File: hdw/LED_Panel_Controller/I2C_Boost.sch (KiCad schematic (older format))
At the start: 2 parts

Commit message: made a lot more schematic progress
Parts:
- C?, U?: Configuration (none) -> DNP
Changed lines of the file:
@@
 F 3 "https://www.analog.com/media/en/technical-documentation/data-sheets/1694fa.pdf" H 5200 4060 60  0001 C CNN
 F 4 "LTC1694CS5#TRPBFCT-ND" H 5400 3510 60  0001 C CNN "Digi-Key PN"
+F 5 "DNP" H 5300 3300 50  0000 C CNN "Configuration"
 	1    5300 3760
 	1    0    0    -1
@@
 F 6 "X7R" H 4190 3680 50  0000 R CNN "Dielectric"
 F 7 "490-10701-1-ND" H 4765 4280 60  0001 C CNN "Digi-Key PN"
+F 8 "DNP" H 4110 3970 50  0000 C CNN "Configuration"
 	1    4340 3780
 	1    0    0    -1

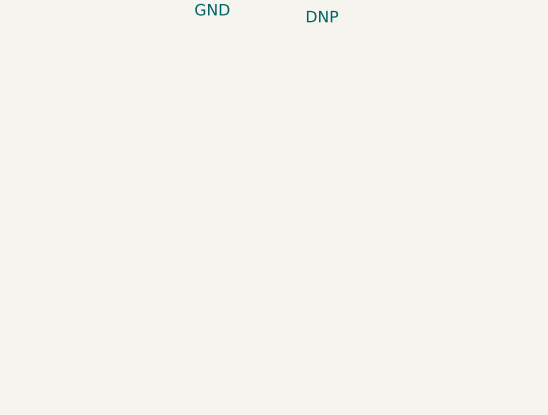
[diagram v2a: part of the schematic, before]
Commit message: assigned a lot of nets to MCU pins
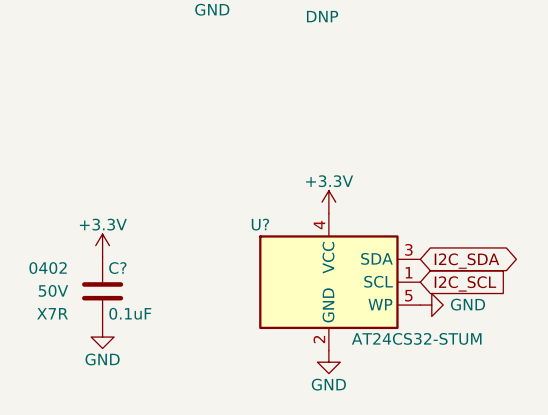
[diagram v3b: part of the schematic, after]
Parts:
- added C?: 0.1uF, Capacitors_SMD:C_0402, symbol Custom_Library:C_Custom
- added U?: AT24CS32-STUM, Package_TO_SOT_SMD:SOT-23-5, symbol Memory_EEPROM:AT24CS32-STUM
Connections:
- net +3V3: now also C?.1, U?.4 (VCC)
- net GND: now also C?.2, U?.2 (GND), U?.5 (WP)
- net I2C_SCL: now also U?.1 (SCL)
- net I2C_SDA: now also U?.3 (SDA)
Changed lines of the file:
@@
 	1    0    0    -1
 $EndComp
+$Comp
+L Memory_EEPROM:AT24CS32-STUM U?
+U 1 1 601A8ABF
+P 5330 5380
+AR Path="/5F5829EF/601A8ABF" Ref="U?"  Part="1"
+AR Path="/5F582A7C/601A8ABF" Ref="U?"  Part="1"
+F 0 "U?" H 5030 5630 50  0000 C CNN
+F 1 "AT24CS32-STUM" H 5430 5130 50  0000 L CNN
+F 2 "Package_TO_SOT_SMD:SOT-23-5" H 5330 5380 50  0001 C CNN
+F 3 "http://ww1.microchip.com/downloads/en/DeviceDoc/Atmel-8869-SEEPROM-AT24CS32-Datasheet.pdf" H 5330 5380 50  0001 C CNN
+	1    5330 5380
+	1    0    0    -1
+$EndComp
+$Comp
+L power:GND #PWR?
+U 1 1 601A8AC5
+P 5330 5680
+AR Path="/5F5829EF/601A8AC5" Ref="#PWR?"  Part="1"
+AR Path="/5F582A7C/601A8AC5" Ref="#PWR?"  Part="1"
+F 0 "#PWR?" H 5330 5430 50  0001 C CNN
+F 1 "GND" H 5330 5530 50  0000 C CNN
+F 2 "" H 5330 5680 50  0001 C CNN
+F 3 "" H 5330 5680 50  0001 C CNN
+	1    5330 5680
+	1    0    0    -1
+$EndComp
+$Comp
+L power:+3.3V #PWR?
+U 1 1 601A8ACB
+P 5330 5080
+AR Path="/5F5829EF/601A8ACB" Ref="#PWR?"  Part="1"
+AR Path="/5F582A7C/601A8ACB" Ref="#PWR?"  Part="1"
+F 0 "#PWR?" H 5330 4930 50  0001 C CNN
+F 1 "+3.3V" H 5330 5220 50  0000 C CNN
+F 2 "" H 5330 5080 50  0001 C CNN
+F 3 "" H 5330 5080 50  0001 C CNN
+	1    5330 5080
+	1    0    0    -1
+$EndComp
+$Comp
+L power:GND #PWR?
+U 1 1 601A97E7
+P 4340 5570
+F 0 "#PWR?" H 4340 5320 50  0001 C CNN
+F 1 "GND" H 4340 5420 50  0000 C CNN
+F 2 "" H 4340 5570 50  0001 C CNN
+F 3 "" H 4340 5570 50  0001 C CNN
+	1    4340 5570
+	1    0    0    -1
+$EndComp
+$Comp
+L Custom_Library:C_Custom C?
+U 1 1 601A97F2
+P 4340 5420
+AR Path="/5BAAE16C/601A97F2" Ref="C?"  Part="1"
+AR Path="/5BB181D8/601A97F2" Ref="C?"  Part="1"
+AR Path="/5BB2595E/601A97F2" Ref="C?"  Part="1"
+AR Path="/5BAAE0FA/601A97F2" Ref="C?"  Part="1"
+AR Path="/5BB86F23/601A97F2" Ref="C?"  Part="1"
+AR Path="/5C1D5C9E/601A97F2" Ref="C?"  Part="1"
+AR Path="/5CB6F1ED/601A97F2" Ref="C?"  Part="1"
+AR Path="/5E939CFF/601A97F2" Ref="C?"  Part="1"
+AR Path="/5E9E0E87/601A97F2" Ref="C?"  Part="1"
+AR Path="/5EAE2D66/601A97F2" Ref="C?"  Part="1"
+AR Path="/5EAE3021/601A97F2" Ref="C?"  Part="1"
+AR Path="/5F582A92/601A97F2" Ref="C?"  Part="1"
+AR Path="/5F582A7C/601A97F2" Ref="C?"  Part="1"
+F 0 "C?" H 4365 5520 50  0000 L CNN
+F 1 "0.1uF" H 4365 5320 50  0000 L CNN
+F 2 "Capacitors_SMD:C_0402" H 4378 5270 50  0001 C CNN
+F 3 "" H 4365 5520 50  0001 C CNN
+F 4 "0402" H 4190 5520 50  0000 R CNN "display_footprint"
+F 5 "50V" H 4190 5420 50  0000 R CNN "Voltage"
+F 6 "X7R" H 4190 5320 50  0000 R CNN "Dielectric"
+F 7 "490-10701-1-ND" H 4765 5920 60  0001 C CNN "Digi-Key PN"
+F 8 "" H 4110 5610 50  0001 C CNN "Configuration"
+	1    4340 5420
+	1    0    0    -1
+$EndComp
+$Comp
+L power:+3.3V #PWR?
+U 1 1 601A97F8
+P 4340 5270
+F 0 "#PWR?" H 4340 5120 50  0001 C CNN
+F 1 "+3.3V" H 4340 5410 50  0000 C CNN
+F 2 "" H 4340 5270 50  0001 C CNN
+F 3 "" H 4340 5270 50  0001 C CNN
+	1    4340 5270
+	1    0    0    -1
+$EndComp
+Text GLabel 5730 5380 2    50   Input ~ 0
+I2C_SCL
+Text GLabel 5730 5280 2    50   BiDi ~ 0
+I2C_SDA
+$Comp
+L power:GND #PWR?
+U 1 1 601AB410
+P 5730 5480
+AR Path="/5F5829EF/601AB410" Ref="#PWR?"  Part="1"
+AR Path="/5F582A7C/601AB410" Ref="#PWR?"  Part="1"
+F 0 "#PWR?" H 5730 5230 50  0001 C CNN
+F 1 "GND" V 5730 5350 50  0000 R CNN
+F 2 "" H 5730 5480 50  0001 C CNN
+F 3 "" H 5730 5480 50  0001 C CNN
+	1    5730 5480
+	0    -1   -1   0
+$EndComp
 $EndSCHEMATC

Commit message: more schematic development
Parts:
- added C?: 0.1uF, Capacitors_SMD:C_0402, symbol Custom_Library:C_Custom
- added DOC?: FIXME, symbol Custom_Library:I2C_Address
- added U?: MCP9804, Package_DFN_QFN:DFN-8-1EP_3x2mm_P0.5mm_EP1.3x1.5mm, symbol Sensor_Temperature:MCP9804_DFN
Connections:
- net +3V3: now also C?.1, U?.8 (VDD)
- net GND: now also C?.2, U?.4 (GND), U?.9 (EP/GND)
- net I2C_SCL: now also U?.2 (SCL)
- net I2C_SDA: now also U?.1 (SDA)
- no-connect marks 0 -> 1
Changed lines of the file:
@@
 Sheet 13 34
 Title "LED Panel Controller"
-Date "2020-12-23"
+Date "2021-03-24"
 Rev "A"
-Comp "Drew Maatman, Logan Wedel"
+Comp "Drew Maatman"
 Comment1 ""
 Comment2 ""
@@
 	0    -1   -1   0
 $EndComp
+$Comp
+L power:GND #PWR?
+U 1 1 6061CC13
+P 5340 2050
+AR Path="/5B3E071A/6061CC13" Ref="#PWR?"  Part="1"
+AR Path="/5E0652BA/6061CC13" Ref="#PWR?"  Part="1"
+AR Path="/5E0A0E29/6061CC13" Ref="#PWR?"  Part="1"
+AR Path="/5E052856/6061CC13" Ref="#PWR?"  Part="1"
+AR Path="/5EAE2D84/6061CC13" Ref="#PWR?"  Part="1"
+AR Path="/5F581B58/6061CC13" Ref="#PWR?"  Part="1"
+AR Path="/5F581B77/6061CC13" Ref="#PWR?"  Part="1"
+AR Path="/5F581BB7/6061CC13" Ref="#PWR?"  Part="1"
+AR Path="/5F582A7C/6061CC13" Ref="#PWR?"  Part="1"
+F 0 "#PWR?" H 5340 1800 50  0001 C CNN
+F 1 "GND" H 5340 1900 50  0000 C CNN
+F 2 "" H 5340 2050 50  0001 C CNN
+F 3 "" H 5340 2050 50  0001 C CNN
+	1    5340 2050
+	-1   0    0    -1
+$EndComp
+Wire Wire Line
+	5340 2050 5340 2010
+Wire Wire Line
+	5340 2010 5340 1970
+Wire Wire Line
+	5340 2010 5240 2010
+Wire Wire Line
+	5240 2010 5240 1970
+Connection ~ 5340 2010
+$Comp
+L power:+3.3V #PWR?
+U 1 1 6061CC1E
+P 5340 970
+AR Path="/5E0652BA/6061CC1E" Ref="#PWR?"  Part="1"
+AR Path="/5E0A0E29/6061CC1E" Ref="#PWR?"  Part="1"
+AR Path="/5E052856/6061CC1E" Ref="#PWR?"  Part="1"
+AR Path="/5EAE2D84/6061CC1E" Ref="#PWR?"  Part="1"
+AR Path="/5F581B58/6061CC1E" Ref="#PWR?"  Part="1"
+AR Path="/5F581B77/6061CC1E" Ref="#PWR?"  Part="1"
+AR Path="/5F581BB7/6061CC1E" Ref="#PWR?"  Part="1"
+AR Path="/5F582A7C/6061CC1E" Ref="#PWR?"  Part="1"
+F 0 "#PWR?" H 5340 820 50  0001 C CNN
+F 1 "+3.3V" H 5340 1110 50  0000 C CNN
+F 2 "" H 5340 970 50  0001 C CNN
+F 3 "" H 5340 970 50  0001 C CNN
+	1    5340 970
+	-1   0    0    -1
+$EndComp
+$Comp
+L Sensor_Temperature:MCP9804_DFN U?
+U 1 1 6061CC26
+P 5340 1470
+AR Path="/5B3E071A/6061CC26" Ref="U?"  Part="1"
+AR Path="/5E0652BA/6061CC26" Ref="U?"  Part="1"
+AR Path="/5E0A0E29/6061CC26" Ref="U?"  Part="1"
+AR Path="/5E052856/6061CC26" Ref="U?"  Part="1"
+AR Path="/5EAE2D84/6061CC26" Ref="U?"  Part="1"
+AR Path="/5F581B58/6061CC26" Ref="U?"  Part="1"
+AR Path="/5F581B77/6061CC26" Ref="U?"  Part="1"
+AR Path="/5F581BB7/6061CC26" Ref="U?"  Part="1"
+AR Path="/5F582A7C/6061CC26" Ref="U?"  Part="1"
+F 0 "U?" H 5090 1920 50  0000 C CNN
+F 1 "MCP9804" H 5740 1920 50  0000 C CNN
+F 2 "Package_DFN_QFN:DFN-8-1EP_3x2mm_P0.5mm_EP1.3x1.5mm" H 4240 970 50  0001 C CNN
+F 3 "http://ww1.microchip.com/downloads/en/DeviceDoc/22203b.pdf" H 5090 1920 50  0001 C CNN
+F 4 "MCP9804T-E/MCCT-ND" H 5340 1470 50  0001 C CNN "Digi-Key PN"
+F 5 "Telemetry" H 5740 2000 50  0000 C CNN "Configuration"
+	1    5340 1470
+	-1   0    0    -1
+$EndComp
+Text GLabel 5740 1270 2    50   Input ~ 0
+I2C_SCL
+Text GLabel 5740 1170 2    50   BiDi ~ 0
+I2C_SDA
+NoConn ~ 4940 1470
+$Comp
+L power:+3.3V #PWR?
+U 1 1 6061CC2F
+P 5340 2470
+AR Path="/5E0652BA/6061CC2F" Ref="#PWR?"  Part="1"
+AR Path="/5E0A0E29/6061CC2F" Ref="#PWR?"  Part="1"
+AR Path="/5E052856/6061CC2F" Ref="#PWR?"  Part="1"
+AR Path="/5EAE2D84/6061CC2F" Ref="#PWR?"  Part="1"
+AR Path="/5F581B58/6061CC2F" Ref="#PWR?"  Part="1"
+AR Path="/5F581B77/6061CC2F" Ref="#PWR?"  Part="1"
+AR Path="/5F581BB7/6061CC2F" Ref="#PWR?"  Part="1"
+AR Path="/5F582A7C/6061CC2F" Ref="#PWR?"  Part="1"
+F 0 "#PWR?" H 5340 2320 50  0001 C CNN
+F 1 "+3.3V" H 5340 2610 50  0000 C CNN
+F 2 "" H 5340 2470 50  0001 C CNN
+F 3 "" H 5340 2470 50  0001 C CNN
+	1    5340 2470
+	1    0    0    -1
+$EndComp
+$Comp
+L power:GND #PWR?
+U 1 1 6061CC35
+P 5340 2770
+AR Path="/5E0652BA/6061CC35" Ref="#PWR?"  Part="1"
+AR Path="/5E0A0E29/6061CC35" Ref="#PWR?"  Part="1"
+AR Path="/5E052856/6061CC35" Ref="#PWR?"  Part="1"
+AR Path="/5EAE2D84/6061CC35" Ref="#PWR?"  Part="1"
+AR Path="/5F581B58/6061CC35" Ref="#PWR?"  Part="1"
+AR Path="/5F581B77/6061CC35" Ref="#PWR?"  Part="1"
+AR Path="/5F581BB7/6061CC35" Ref="#PWR?"  Part="1"
+AR Path="/5F582A7C/6061CC35" Ref="#PWR?"  Part="1"
+F 0 "#PWR?" H 5340 2520 50  0001 C CNN
+F 1 "GND" H 5340 2620 50  0000 C CNN
+F 2 "" H 5340 2770 50  0001 C CNN
+F 3 "" H 5340 2770 50  0001 C CNN
+	1    5340 2770
+	1    0    0    -1
+$EndComp
+$Comp
+L Custom_Library:I2C_Address DOC?
+U 1 1 6061CC3B
+P 6240 2490
+AR Path="/5E0652BA/6061CC3B" Ref="DOC?"  Part="1"
+AR Path="/5E0A0E29/6061CC3B" Ref="DOC?"  Part="1"
+AR Path="/5E052856/6061CC3B" Ref="DOC?"  Part="1"
+AR Path="/5EAE2D84/6061CC3B" Ref="DOC?"  Part="1"
+AR Path="/5F581B58/6061CC3B" Ref="DOC?"  Part="1"
+AR Path="/5F581B77/6061CC3B" Ref="DOC?"  Part="1"
+AR Path="/5F581BB7/6061CC3B" Ref="DOC?"  Part="1"
+AR Path="/5F582A7C/6061CC3B" Ref="DOC?"  Part="1"
+F 0 "DOC?" H 6240 2740 60  0001 C CNN
+F 1 "FIXME" H 5790 2490 60  0000 L CNN
+F 2 "" H 6240 2840 60  0001 C CNN
+F 3 "" H 6240 2840 60  0001 C CNN
+	1    6240 2490
+	1    0    0    -1
+$EndComp
+$Comp
+L Custom_Library:C_Custom C?
+U 1 1 6061CC45
+P 5340 2620
+AR Path="/5B3E071A/6061CC45" Ref="C?"  Part="1"
+AR Path="/5E0652BA/6061CC45" Ref="C?"  Part="1"
+AR Path="/5E0A0E29/6061CC45" Ref="C?"  Part="1"
+AR Path="/5E052856/6061CC45" Ref="C?"  Part="1"
+AR Path="/5EAE2D84/6061CC45" Ref="C?"  Part="1"
+AR Path="/5F581B58/6061CC45" Ref="C?"  Part="1"
+AR Path="/5F581B77/6061CC45" Ref="C?"  Part="1"
+AR Path="/5F581BB7/6061CC45" Ref="C?"  Part="1"
+AR Path="/5F582A7C/6061CC45" Ref="C?"  Part="1"
+F 0 "C?" H 5365 2720 50  0000 L CNN
+F 1 "0.1uF" H 5365 2520 50  0000 L CNN
+F 2 "Capacitors_SMD:C_0402" H 5378 2470 50  0001 C CNN
+F 3 "" H 5365 2720 50  0001 C CNN
+F 4 "0402" H 5190 2680 50  0000 R CNN "display_footprint"
+F 5 "50V" H 5190 2580 50  0000 R CNN "Voltage"
+F 6 "X7R" H 5190 2480 50  0000 R CNN "Dielectric"
+F 7 "Telemetry" H 5190 2770 50  0000 R CNN "Configuration"
+	1    5340 2620
+	1    0    0    -1
+$EndComp
 $EndSCHEMATC

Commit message: added digikey pns, footprints, bom scrubbed
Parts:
- C?: Digi-Key PN (none) -> 490-10701-1-ND
- U?: Digi-Key PN (none) -> AT24CS32-STUM-T
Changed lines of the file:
@@
 F 2 "Package_TO_SOT_SMD:SOT-23-5" H 5330 5380 50  0001 C CNN
 F 3 "http://ww1.microchip.com/downloads/en/DeviceDoc/Atmel-8869-SEEPROM-AT24CS32-Datasheet.pdf" H 5330 5380 50  0001 C CNN
+F 4 "AT24CS32-STUM-T" H 5330 5380 50  0001 C CNN "Digi-Key PN"
 	1    5330 5380
 	1    0    0    -1
@@
 F 6 "X7R" H 5190 2480 50  0000 R CNN "Dielectric"
 F 7 "Telemetry" H 5190 2770 50  0000 R CNN "Configuration"
+F 8 "490-10701-1-ND" H 5340 2620 50  0001 C CNN "Digi-Key PN"
 	1    5340 2620
 	1    0    0    -1
